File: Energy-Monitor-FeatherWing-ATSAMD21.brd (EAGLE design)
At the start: 50.8 x 22.9 mm, 32 parts

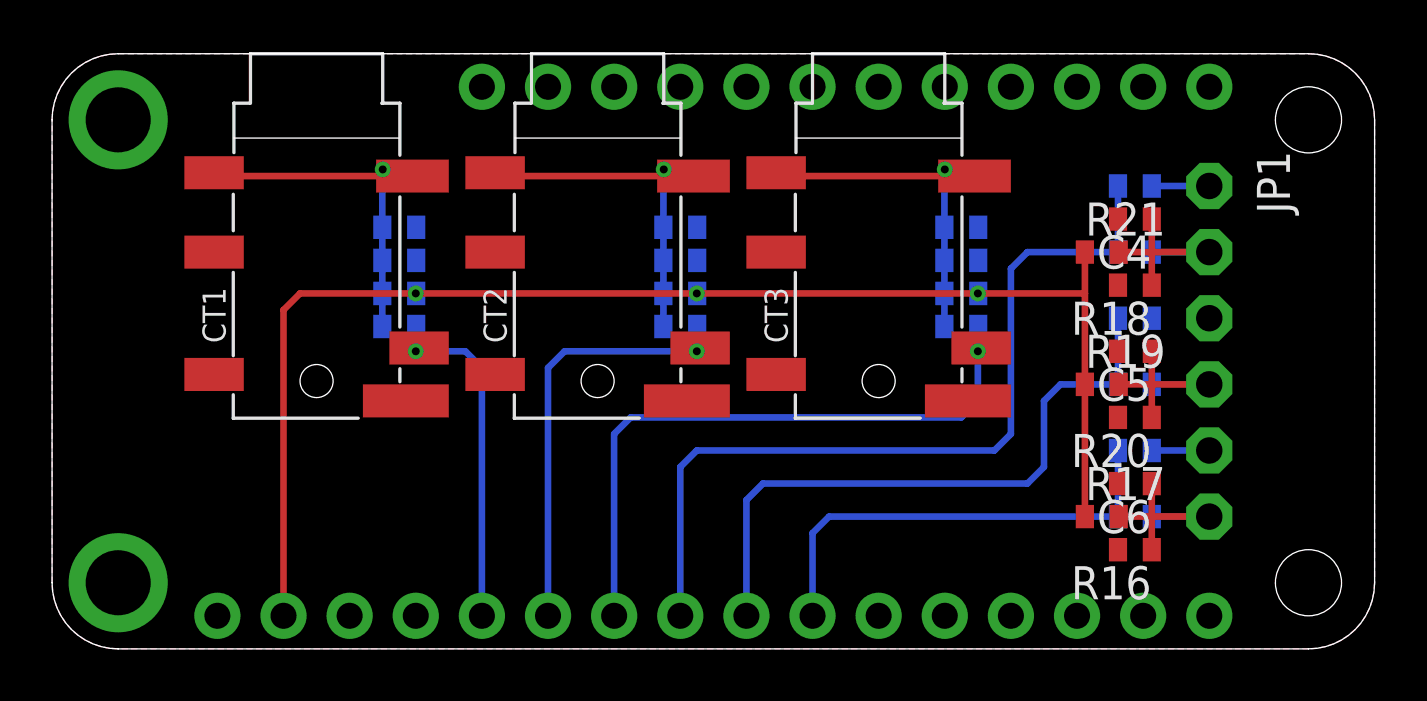
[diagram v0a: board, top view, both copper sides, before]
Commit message: Clean up layout and component names
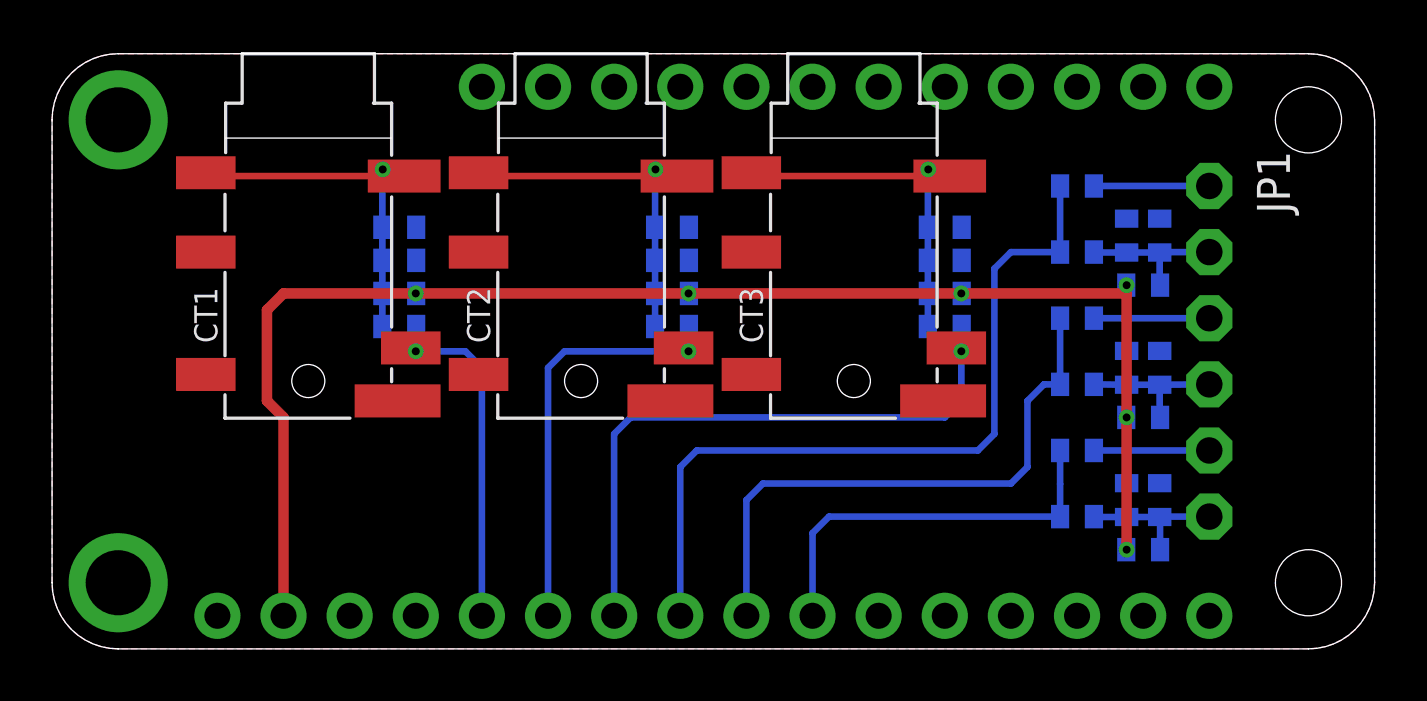
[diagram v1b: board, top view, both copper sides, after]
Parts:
- R12: value 100k -> 470k
- R13: value 10 -> 470k
- R18: value 470k -> 100k
- R19: value 470k -> 10
- R7: value 22 -> 470k
- R9: value 470k -> 22
- moved R21 11.5 mm to (41.9, 3.81), flipped to the bottom, turned to 180 degrees
- moved R16 6.99 mm to (41.3, 10.8), flipped to the bottom, turned to 90 degrees
- moved R18 6.73 mm to (39.4, 7.62), flipped to the bottom
- moved R15 5.54 mm to (39.4, 10.2)
- moved R14 5.54 mm to (39.4, 12.7)
- moved R19 5.17 mm to (39.4, 5.08), flipped to the bottom, turned to 180 degrees
- moved R17 4.13 mm to (41.9, 8.89), flipped to the bottom, turned to 180 degrees
- moved R13 3.82 mm to (41.9, 14.0)
- moved R12 3.19 mm to (41.3, 15.9), turned to 90 degrees
- moved R20 3.19 mm to (41.3, 5.71), flipped to the bottom, turned to 90 degrees
- moved R7 2.62 mm to (34.3, 14.9)
- moved R10 2.22 mm to (39.4, 17.8)
- moved R11 2.22 mm to (39.4, 15.2)
- moved R8 1.42 mm to (34.3, 13.7)
- moved R9 1.42 mm to (34.3, 12.4)
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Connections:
- net GND: now also R12.2, R7.1; no longer R18.2, R8.1
- net N$10: now also R18.2; no longer R14.2
- net N$11: now also R18.1, R19.1; no longer R14.1, R15.1
- net N$13: now also R15.2, R16.1, R17.2; no longer R13.2, R19.2, R20.1
- net N$3: now also R9.1; no longer R7.1
- net N$6: now also R19.2, R20.1, R21.2; no longer R15.2, R16.1, R17.2
- net N$7: now also R14.2; no longer R12.2
- net N$8: now also R14.1, R15.1; no longer R12.1, R13.1
- net N$9: now also R12.1, R13.2; no longer R18.1, R21.2
- net VCC: now also R13.1, R8.1; no longer R19.1, R9.1
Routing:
- net N$7: track 0.00 -> 4.43 mm
- net VCC: track 53.0 -> 55.5 mm, vias 3 -> 6
- net N$13: track 8.23 -> 5.70 mm
- net N$9: track 8.23 -> 5.70 mm
- net N$6: track 8.23 -> 5.73 mm
- net N$5: track 32.2 -> 30.0 mm
- net N$8: track 24.6 -> 22.4 mm
- net N$11: track 17.7 -> 15.5 mm
- net N$4: track 2.21 -> 4.43 mm
- net N$10: track 2.21 -> 4.43 mm

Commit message: Initial work on adding 3-phase bridge rectifier
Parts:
- added U1: SDA006-7, Diodes_Inc_By_element14_Batch_1:SOT65P210X100-6N
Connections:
- removed net N$13: C5.1, JP1.4, R15.2, R16.1, R17.2
- removed net N$6: C6.1, JP1.6, R19.2, R20.1, R21.2
- removed net N$9: C4.1, JP1.2, R11.2, R12.1, R13.2
- new net 12V: U1.4, U1.5
- new net AC_GND: C4.1, C5.1, C6.1, JP1.2, JP1.4, JP1.6, R11.2, R12.1, R13.2, R15.2, R16.1, R17.2, R19.2, R20.1, R21.2
- net GND: now also U1.2
- net N$10: now also U1.6
- net N$4: now also U1.3
- net N$7: now also U1.1
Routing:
- net AC_GND: track 0.00 -> 32.1 mm
- net N$4: track 4.43 -> 13.9 mm
- net N$6: track 5.73 -> 0.00 mm
- net N$9: track 5.70 -> 0.00 mm
- net N$13: track 5.70 -> 0.00 mm
- net N$10: track 4.43 -> 7.53 mm
- net N$7: track 4.43 -> 7.53 mm
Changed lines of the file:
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@@
 <?xml version="1.0" encoding="utf-8"?>
 <!DOCTYPE eagle SYSTEM "eagle.dtd">
-<eagle version="7.5.0">
+<eagle version="7.6.0">
 <drawing>
 <settings>
@@
 </element>
 <element name="C4" library="resistor" package="C0402" value="10" x="42.545" y="15.875" smashed="yes" rot="MR90">
-<attribute name="NAME" x="45.72" y="16.51" size="0.8128" layer="26" rot="MR180" align="center-left"/>
+<attribute name="NAME" x="45.72" y="14.9225" size="0.8128" layer="26" rot="MR180" align="center-left"/>
 <attribute name="VALUE" x="40.64" y="15.24" size="1.27" layer="28" rot="MR90"/>
 </element>
 <element name="C5" library="resistor" package="C0402" value="10" x="42.545" y="10.795" smashed="yes" rot="MR90">
-<attribute name="NAME" x="45.72" y="11.43" size="0.8128" layer="26" rot="MR180" align="center-left"/>
+<attribute name="NAME" x="45.72" y="13.97" size="0.8128" layer="26" rot="MR180" align="center-left"/>
 <attribute name="VALUE" x="40.64" y="10.16" size="1.27" layer="28" rot="MR90"/>
 </element>
 <element name="C6" library="resistor" package="C0402" value="10" x="42.545" y="5.715" smashed="yes" rot="MR90">
-<attribute name="NAME" x="45.72" y="6.35" size="0.8128" layer="26" rot="MR180" align="center-left"/>
+<attribute name="NAME" x="45.72" y="13.0175" size="0.8128" layer="26" rot="MR180" align="center-left"/>
 <attribute name="VALUE" x="40.64" y="5.08" size="1.27" layer="28" rot="MR90"/>
 </element>
@@
 <attribute name="NAME" x="40.64" y="13.97" size="0.8128" layer="26" rot="MR180" align="center-right"/>
 <attribute name="VALUE" x="41.275" y="15.875" size="1.27" layer="28" rot="MR180"/>
+</element>
+<element name="U1" library="Diodes_Inc_By_element14_Batch_1" package="SOT65P210X100-6N" value="SDA006-7" x="46.99" y="10.16" rot="MR270">
+<attribute name="PACKAGE" value="TSOT-23-6" x="46.99" y="10.16" size="1.778" layer="28" rot="MR270" display="off"/>
+<attribute name="SUPPLIER" value="DIODES INC." x="46.99" y="10.16" size="1.778" layer="28" rot="MR270" display="off"/>
+<attribute name="MPN" value="SDA006-7" x="46.99" y="10.16" size="1.778" layer="28" rot="MR270" display="off"/>
 </element>
 </elements>
@@
 <vertex x="50.8" y="2.54" curve="-90"/>
 </polygon>
+<contactref element="U1" pad="2"/>
 </signal>
 <signal name="VCC">
@@
 <contactref element="R10" pad="2"/>
 <wire x1="40.02" y1="17.78" x2="44.45" y2="17.78" width="0.254" layer="16"/>
+<contactref element="U1" pad="3"/>
+<wire x1="44.45" y1="17.7927" x2="46.9773" y2="17.7927" width="0.254" layer="16"/>
+<wire x1="46.9773" y1="17.7927" x2="47.625" y2="17.145" width="0.254" layer="16"/>
+<wire x1="47.625" y1="17.145" x2="47.625" y2="11.1506" width="0.254" layer="16"/>
+<wire x1="47.625" y1="11.1506" x2="47.6504" y2="11.1252" width="0.254" layer="16"/>
+<wire x1="44.45" y1="17.7927" x2="44.45" y2="17.78" width="0" layer="19" extent="16-16"/>
 </signal>
 <signal name="N$5">
@@
 <contactref element="R14" pad="2"/>
 <wire x1="40.02" y1="12.7" x2="44.45" y2="12.7" width="0.254" layer="16"/>
+<contactref element="U1" pad="1"/>
+<wire x1="46.3296" y1="11.1252" x2="46.3296" y2="12.0904" width="0.254" layer="16"/>
+<wire x1="46.3296" y1="12.0904" x2="45.72" y2="12.7" width="0.254" layer="16"/>
+<wire x1="45.72" y1="12.7" x2="44.45" y2="12.7" width="0.254" layer="16"/>
 </signal>
 <signal name="N$8">
@@
 <wire x1="26.67" y1="5.715" x2="26.67" y2="1.27" width="0.254" layer="16"/>
 </signal>
-<signal name="N$9">
+<signal name="AC_GND">
 <contactref element="C4" pad="1"/>
 <contactref element="R11" pad="2"/>
@@
 <wire x1="41.275" y1="15.225" x2="40.035" y2="15.225" width="0.254" layer="16"/>
 <wire x1="40.035" y1="15.225" x2="40.02" y2="15.24" width="0.254" layer="16"/>
-</signal>
-<signal name="N$10">
-<contactref element="R18" pad="2"/>
-<contactref element="JP1" pad="5"/>
-<wire x1="44.45" y1="7.62" x2="40.02" y2="7.62" width="0.254" layer="16"/>
-</signal>
-<signal name="N$11">
-<contactref element="R18" pad="1"/>
-<contactref element="R19" pad="1"/>
-<contactref element="MS1" pad="10"/>
-<wire x1="38.72" y1="5.08" x2="29.845" y2="5.08" width="0.254" layer="16"/>
-<wire x1="29.845" y1="5.08" x2="29.21" y2="4.445" width="0.254" layer="16"/>
-<wire x1="29.21" y1="4.445" x2="29.21" y2="1.27" width="0.254" layer="16"/>
-<wire x1="38.72" y1="7.62" x2="38.72" y2="6.335" width="0.254" layer="16"/>
-<wire x1="38.72" y1="6.335" x2="38.72" y2="5.08" width="0.254" layer="16"/>
-</signal>
-<signal name="N$13">
-<contactref element="C5" pad="1"/>
-<contactref element="R15" pad="2"/>
-<contactref element="JP1" pad="4"/>
-<contactref element="R16" pad="1"/>
-<contactref element="R17" pad="2"/>
-<wire x1="42.56" y1="8.89" x2="42.545" y2="8.89" width="0.254" layer="16"/>
-<wire x1="42.545" y1="8.89" x2="42.545" y2="10.145" width="0.254" layer="16"/>
-<wire x1="44.45" y1="10.16" x2="42.545" y2="10.145" width="0.254" layer="16"/>
-<wire x1="42.545" y1="10.145" x2="41.275" y2="10.145" width="0.254" layer="16"/>
-<wire x1="41.275" y1="10.145" x2="40.02" y2="10.16" width="0.254" layer="16"/>
-</signal>
-<signal name="N$6">
 <contactref element="R19" pad="2"/>
 <contactref element="JP1" pad="6"/>
@@
 <wire x1="42.545" y1="5.065" x2="42.56" y2="5.065" width="0.254" layer="16"/>
 <wire x1="42.56" y1="5.065" x2="42.56" y2="3.81" width="0.254" layer="16"/>
+<contactref element="C5" pad="1"/>
+<contactref element="R15" pad="2"/>
+<contactref element="JP1" pad="4"/>
+<contactref element="R16" pad="1"/>
+<contactref element="R17" pad="2"/>
+<wire x1="42.56" y1="8.89" x2="42.545" y2="8.89" width="0.254" layer="16"/>
+<wire x1="42.545" y1="8.89" x2="42.545" y2="10.145" width="0.254" layer="16"/>
+<wire x1="44.45" y1="10.16" x2="42.545" y2="10.145" width="0.254" layer="16"/>
+<wire x1="42.545" y1="10.145" x2="41.275" y2="10.145" width="0.254" layer="16"/>
+<wire x1="41.275" y1="10.145" x2="40.02" y2="10.16" width="0.254" layer="16"/>
+<wire x1="44.45" y1="10.145" x2="44.45" y2="10.16" width="0.254" layer="16"/>
+<wire x1="46.0375" y1="15.24" x2="46.0375" y2="10.16" width="0.254" layer="1"/>
+<wire x1="46.0375" y1="10.16" x2="46.0375" y2="5.08" width="0.254" layer="1"/>
+<wire x1="46.0375" y1="15.24" x2="44.45" y2="15.24" width="0.254" layer="1"/>
+<wire x1="46.0375" y1="5.08" x2="44.45" y2="5.08" width="0.254" layer="1"/>
+<wire x1="46.0375" y1="10.16" x2="44.45" y2="10.16" width="0.254" layer="1"/>
+</signal>
+<signal name="N$10">
+<contactref element="R18" pad="2"/>
+<contactref element="JP1" pad="5"/>
+<wire x1="44.45" y1="7.62" x2="40.02" y2="7.62" width="0.254" layer="16"/>
+<contactref element="U1" pad="6"/>
+<wire x1="46.3296" y1="9.1948" x2="46.3296" y2="8.2296" width="0.254" layer="16"/>
+<wire x1="46.3296" y1="8.2296" x2="45.72" y2="7.62" width="0.254" layer="16"/>
+<wire x1="45.72" y1="7.62" x2="44.45" y2="7.62" width="0.254" layer="16"/>
+</signal>
+<signal name="N$11">
+<contactref element="R18" pad="1"/>
+<contactref element="R19" pad="1"/>
+<contactref element="MS1" pad="10"/>
+<wire x1="38.72" y1="5.08" x2="29.845" y2="5.08" width="0.254" layer="16"/>
+<wire x1="29.845" y1="5.08" x2="29.21" y2="4.445" width="0.254" layer="16"/>
+<wire x1="29.21" y1="4.445" x2="29.21" y2="1.27" width="0.254" layer="16"/>
+<wire x1="38.72" y1="7.62" x2="38.72" y2="6.335" width="0.254" layer="16"/>
+<wire x1="38.72" y1="6.335" x2="38.72" y2="5.08" width="0.254" layer="16"/>
+</signal>
+<signal name="12V">
+<contactref element="U1" pad="4"/>
+<contactref element="U1" pad="5"/>
+<wire x1="46.99" y1="9.1948" x2="47.6504" y2="9.1948" width="0" layer="19" extent="16-16"/>
 </signal>
 </signals>
